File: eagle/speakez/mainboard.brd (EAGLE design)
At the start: 29 parts, among them U1 +12v

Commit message: added DAC cap + resistor
didn't choose cap value yet. Sent output to a header test pin
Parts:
- removed TESTPINS1: (no value), pinhead:1X05M
- added C9: (no value), SparkFun-Capacitors:0805
- added R5: 50k, SparkFun-Passives:0805
- TESTPINS: device pinhead:1X05M -> pinhead:1X07
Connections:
- new net N$27: C9.2, U$1.18
- new net N$28: C9.1, R5.2, TESTPINS.7
- net GND: now also R5.1, TESTPINS.6
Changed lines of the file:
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@@
 <element name="R1" library="rcl" package="M0805" value="5kohm" x="63.5" y="36.83"/>
 <element name="R2" library="rcl" package="M0805" value="5kohm" x="63.5" y="31.75"/>
-<element name="TESTPINS" library="pinhead" package="1X05M" value="" x="58.42" y="39.37" rot="R90"/>
+<element name="TESTPINS" library="pinhead" package="1X07" value="" x="58.42" y="39.37" rot="R90"/>
 <element name="TOAMBIENT" library="pinhead" package="1X04M" value="" x="63.5" y="46.99"/>
 <element name="VOICE" library="InvenSense-INMP621ACEZ-R7" package="ADI_ADMP521A" value="ADMP621ACEZ-RL7" x="63.5" y="17.78">
@@
 </element>
 <element name="C3" library="SparkFun-Capacitors" package="0805" value="0.1uF" x="-22.86" y="6.35"/>
-<element name="TESTPINS1" library="pinhead" package="1X05M" value="" x="-16.51" y="0"/>
 <element name="U$1" library="Teensy_DIY_v1.0" package="QFP50P1200X1200X160-64N" value="MK20DX256VLH7" x="-20.32" y="-15.24"/>
 <element name="JP1" library="pinhead" package="1X16" value="" x="0" y="-30.48"/>
@@
 <element name="PROGRAMMER" library="pel_hdr" package="PH005-1-5" value="PH1X5-05" x="-55.88" y="-95.25"/>
 <element name="SERIAL" library="pinhead" package="1X04" value="" x="-50.8" y="-109.22"/>
+<element name="R5" library="SparkFun-Passives" package="0805" value="50k" x="-64.77" y="-114.3"/>
+<element name="C9" library="SparkFun-Capacitors" package="0805" value="" x="-68.58" y="-114.3"/>
 </elements>
 <signals>
@@
 <contactref element="R1" pad="2"/>
 <contactref element="C1" pad="1"/>
-<contactref element="TESTPINS" pad="4"/>
 <contactref element="U$1" pad="38"/>
 <contactref element="U$1" pad="11"/>
-<wire x1="58.42" y1="41.37" x2="62.55" y2="41.91" width="0" layer="19" extent="1-1"/>
+<contactref element="TESTPINS" pad="4"/>
+<wire x1="58.42" y1="39.37" x2="62.55" y2="41.91" width="0" layer="19" extent="1-1"/>
 <wire x1="64.45" y1="36.83" x2="62.55" y2="41.91" width="0" layer="19" extent="1-1"/>
-<wire x1="-14.605" y1="-16.4846" x2="58.42" y2="41.37" width="0" layer="19" extent="1-1"/>
+<wire x1="-14.605" y1="-16.4846" x2="58.42" y2="39.37" width="0" layer="19" extent="1-1"/>
 <wire x1="-26.035" y1="-16.4846" x2="-14.605" y2="-16.4846" width="0" layer="19" extent="1-1"/>
 </signal>
@@
 <contactref element="R2" pad="2"/>
 <contactref element="C2" pad="1"/>
-<contactref element="TESTPINS" pad="5"/>
 <contactref element="U$1" pad="37"/>
 <contactref element="U$1" pad="12"/>
-<wire x1="64.45" y1="31.75" x2="58.42" y2="43.37" width="0" layer="19" extent="1-1"/>
+<contactref element="TESTPINS" pad="5"/>
+<wire x1="64.45" y1="31.75" x2="58.42" y2="41.91" width="0" layer="19" extent="1-1"/>
 <wire x1="62.55" y1="26.67" x2="64.45" y2="31.75" width="0" layer="19" extent="1-1"/>
 <wire x1="-14.605" y1="-16.9926" x2="62.55" y2="26.67" width="0" layer="19" extent="1-1"/>
@@
 <contactref element="TOAMBIENT" pad="3"/>
 <contactref element="R3" pad="1"/>
+<contactref element="R5" pad="1"/>
+<contactref element="TESTPINS" pad="6"/>
+<wire x1="-58.05" y1="-86.36" x2="-65.67" y2="-114.3" width="0" layer="19" extent="1-1"/>
 <wire x1="61.7728" y1="17.78" x2="-58.05" y2="-86.36" width="0" layer="19" extent="1-1"/>
 <wire x1="62.5348" y1="17.78" x2="61.7728" y2="17.78" width="0" layer="19" extent="1-1"/>
@@
 <wire x1="64.45" y1="41.91" x2="64.45" y2="26.67" width="0" layer="19" extent="1-1"/>
 <wire x1="64.5" y1="46.99" x2="64.45" y2="41.91" width="0" layer="19" extent="1-1"/>
+<wire x1="58.42" y1="44.45" x2="64.45" y2="41.91" width="0" layer="19" extent="1-1"/>
 </signal>
 <signal name="N$4">
 <contactref element="VOICE" pad="5"/>
 <contactref element="R2" pad="1"/>
-<contactref element="TESTPINS" pad="3"/>
 <contactref element="U$1" pad="36"/>
 <contactref element="U$1" pad="9"/>
-<wire x1="62.55" y1="31.75" x2="58.42" y2="39.37" width="0" layer="19" extent="1-1"/>
+<contactref element="TESTPINS" pad="3"/>
+<wire x1="62.55" y1="31.75" x2="58.42" y2="36.83" width="0" layer="19" extent="1-1"/>
 <wire x1="64.6176" y1="17.3228" x2="62.55" y2="31.75" width="0" layer="19" extent="1-1"/>
 <wire x1="-14.605" y1="-17.5006" x2="64.6176" y2="17.3228" width="0" layer="19" extent="1-1"/>
@@
 </signal>
 <signal name="TEST-PINS">
-<contactref element="TESTPINS" pad="1"/>
 <contactref element="VOICE" pad="1"/>
 <contactref element="TOAMBIENT" pad="2"/>
-<wire x1="58.42" y1="35.37" x2="62.5" y2="46.99" width="0" layer="19" extent="1-1"/>
-<wire x1="64.6176" y1="18.2372" x2="58.42" y2="35.37" width="0" layer="19" extent="1-1"/>
+<contactref element="TESTPINS" pad="1"/>
+<wire x1="58.42" y1="31.75" x2="62.5" y2="46.99" width="0" layer="19" extent="1-1"/>
+<wire x1="64.6176" y1="18.2372" x2="58.42" y2="31.75" width="0" layer="19" extent="1-1"/>
 </signal>
 <signal name="N$5">
@@
 <signal name="N$10">
 <contactref element="TOAMBIENT" pad="4"/>
-<contactref element="TESTPINS" pad="2"/>
 <contactref element="R1" pad="1"/>
 <contactref element="U$1" pad="10"/>
+<contactref element="TESTPINS" pad="2"/>
 <wire x1="62.55" y1="36.83" x2="66.5" y2="46.99" width="0" layer="19" extent="1-1"/>
-<wire x1="58.42" y1="37.37" x2="62.55" y2="36.83" width="0" layer="19" extent="1-1"/>
-<wire x1="-26.035" y1="-16.002" x2="58.42" y2="37.37" width="0" layer="19" extent="1-1"/>
+<wire x1="58.42" y1="34.29" x2="62.55" y2="36.83" width="0" layer="19" extent="1-1"/>
+<wire x1="-26.035" y1="-16.002" x2="58.42" y2="34.29" width="0" layer="19" extent="1-1"/>
 </signal>
 <signal name="N$9">
@@
 <wire x1="-26.035" y1="-11.9888" x2="-52.07" y2="-109.22" width="0" layer="19" extent="1-1"/>
 </signal>
+<signal name="N$27">
+<contactref element="U$1" pad="18"/>
+<contactref element="C9" pad="2"/>
+<wire x1="-23.5712" y1="-20.955" x2="-67.68" y2="-114.3" width="0" layer="19" extent="1-1"/>
+</signal>
+<signal name="N$28">
+<contactref element="C9" pad="1"/>
+<contactref element="R5" pad="2"/>
+<contactref element="TESTPINS" pad="7"/>
+<wire x1="-63.87" y1="-114.3" x2="-69.48" y2="-114.3" width="0" layer="19" extent="1-1"/>
+<wire x1="58.42" y1="46.99" x2="-63.87" y2="-114.3" width="0" layer="19" extent="1-1"/>
+</signal>
 </signals>

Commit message: test pins for VCC and RESET
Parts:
- removed JP1, JP2, JP3, JP4: (no value), pinhead:1X16
- added TEST2: (no value), pinhead:1X05
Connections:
- net N$16: now also TEST2.1
- net N$20: now also TEST2.2
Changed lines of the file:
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@@
 <element name="C3" library="SparkFun-Capacitors" package="0805" value="0.1uF" x="-22.86" y="6.35"/>
 <element name="U$1" library="Teensy_DIY_v1.0" package="QFP50P1200X1200X160-64N" value="MK20DX256VLH7" x="-20.32" y="-15.24"/>
-<element name="JP1" library="pinhead" package="1X16" value="" x="0" y="-30.48"/>
-<element name="JP2" library="pinhead" package="1X16" value="" x="0" y="-45.72"/>
-<element name="JP3" library="pinhead" package="1X16" value="" x="0" y="-60.96"/>
-<element name="JP4" library="pinhead" package="1X16" value="" x="0" y="-76.2"/>
 <element name="U1" library="SparkFun-PowerIC" package="TO-252" value="+12v" x="-34.29" y="-74.93">
 <attribute name="PROD_ID" value="VREG-12370" x="-34.29" y="-74.93" size="1.778" layer="27" display="off"/>
@@
 <element name="R5" library="SparkFun-Passives" package="0805" value="50k" x="-64.77" y="-114.3"/>
 <element name="C9" library="SparkFun-Capacitors" package="0805" value="" x="-68.58" y="-114.3"/>
+<element name="TEST2" library="pinhead" package="1X05" value="" x="-57.15" y="-124.46"/>
 </elements>
 <signals>
@@
 <contactref element="R4" pad="1"/>
 <contactref element="SERIAL" pad="3"/>
+<contactref element="TEST2" pad="1"/>
+<wire x1="-49.53" y1="-109.22" x2="-62.23" y2="-124.46" width="0" layer="19" extent="1-1"/>
 <wire x1="-61.86" y1="-86.36" x2="-49.53" y2="-109.22" width="0" layer="19" extent="1-1"/>
 <wire x1="-54.24" y1="-81.28" x2="-61.86" y2="-86.36" width="0" layer="19" extent="1-1"/>
@@
 <contactref element="R4" pad="2"/>
 <contactref element="PROGRAMMER" pad="1"/>
+<contactref element="TEST2" pad="2"/>
+<wire x1="-55.88" y1="-95.25" x2="-59.69" y2="-124.46" width="0" layer="19" extent="1-1"/>
 <wire x1="-60.06" y1="-86.36" x2="-55.88" y2="-95.25" width="0" layer="19" extent="1-1"/>
 <wire x1="-14.605" y1="-18.4912" x2="-60.06" y2="-86.36" width="0" layer="19" extent="1-1"/>

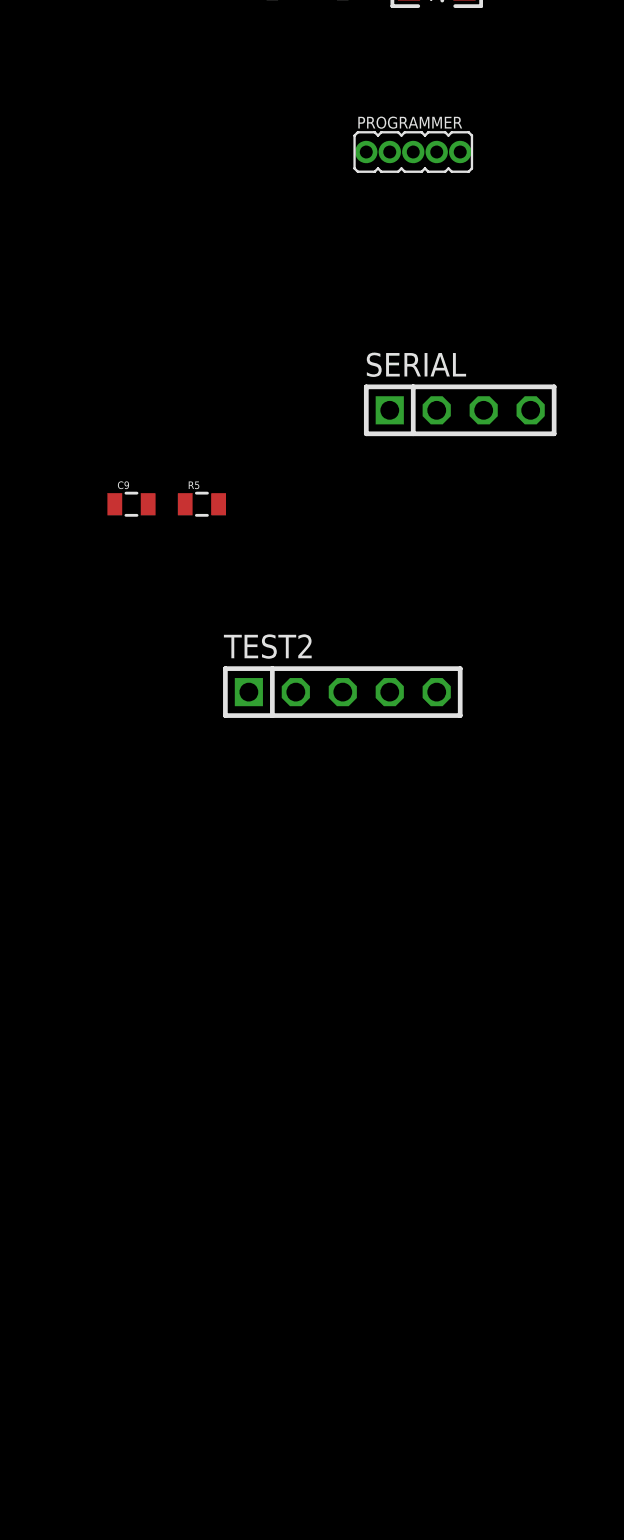
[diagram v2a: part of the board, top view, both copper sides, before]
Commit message: Added correct header for programmer
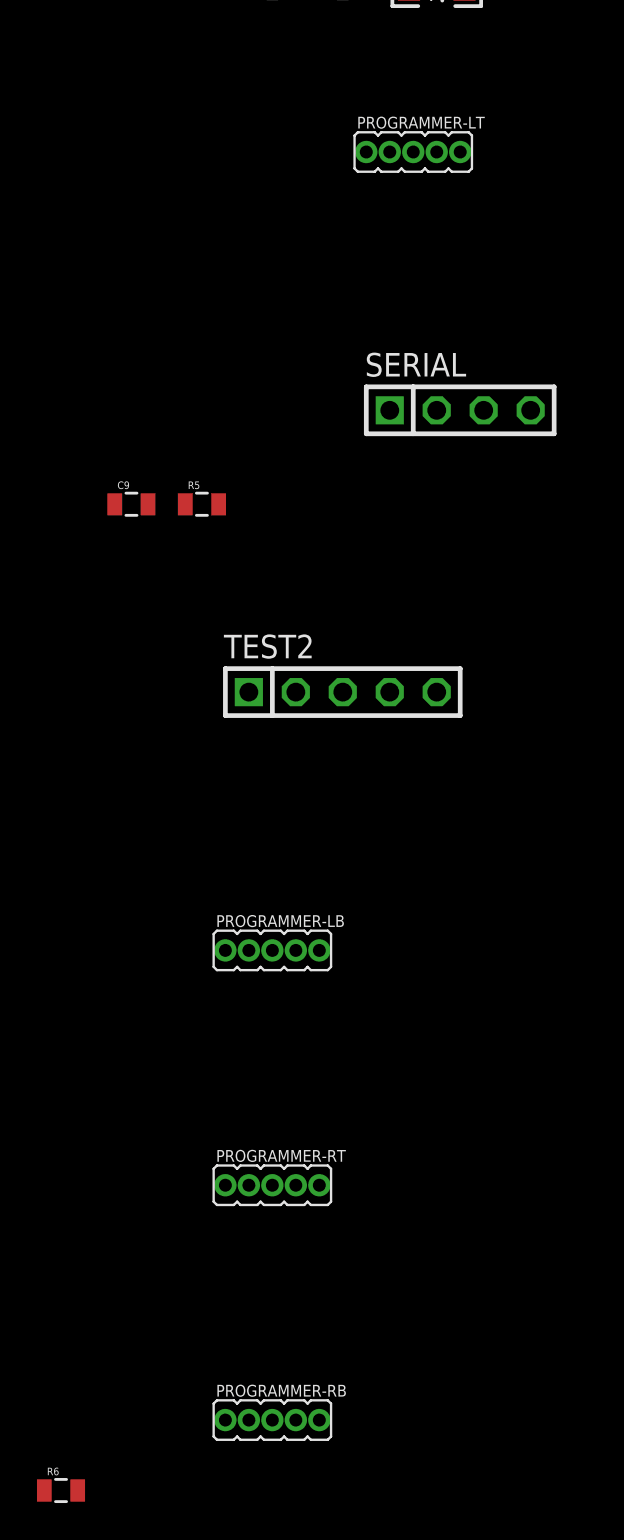
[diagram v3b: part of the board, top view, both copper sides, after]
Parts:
- added PROGRAMMER-LB, PROGRAMMER-RB, PROGRAMMER-RT: PH1X5-05, pel_hdr:PH005-1-5
- added R6: 100k, SparkFun-Passives:0805
- renumbered PROGRAMMER to PROGRAMMER-LT
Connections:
- removed net N$22: PROGRAMMER-LT.3, U$1.23
- new net N$29: BATTERY.2, C6.2, C7.2, C8.2, PROGRAMMER-RB.1, PROGRAMMER-RB.2, PROGRAMMER-RB.3, PROGRAMMER-RB.4, PROGRAMMER-RB.5, PROGRAMMER-RT.2, PROGRAMMER-RT.3, PROGRAMMER-RT.4, PROGRAMMER-RT.5, SERIAL.4, U$1.31, U$1.4, U$1.47, U1.3
- net N$14: now also PROGRAMMER-LT.5, U$1.22; no longer BATTERY.2, C6.2, C7.2, C8.2, SERIAL.4, U$1.31, U$1.4, U$1.47, U1.3
- net N$16: now also PROGRAMMER-LT.1, R6.1
- net N$20: now also PROGRAMMER-LB.3; no longer PROGRAMMER-LT.1
- net N$21: now also PROGRAMMER-LB.4, U$1.23; no longer PROGRAMMER-LT.2, U$1.22
- net N$23: now also PROGRAMMER-LT.3; no longer PROGRAMMER-LT.4
- net N$24: now also PROGRAMMER-LT.4, R6.2; no longer PROGRAMMER-LT.5
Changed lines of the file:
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@@
 <element name="R3" library="SparkFun-Passives" package="0805" value="66 ohms" x="-57.15" y="-86.36"/>
 <element name="R4" library="SparkFun-Passives" package="0805" value="10k" x="-60.96" y="-86.36"/>
-<element name="PROGRAMMER" library="pel_hdr" package="PH005-1-5" value="PH1X5-05" x="-55.88" y="-95.25"/>
+<element name="PROGRAMMER-LT" library="pel_hdr" package="PH005-1-5" value="PH1X5-05" x="-55.88" y="-95.25"/>
 <element name="SERIAL" library="pinhead" package="1X04" value="" x="-50.8" y="-109.22"/>
 <element name="R5" library="SparkFun-Passives" package="0805" value="50k" x="-64.77" y="-114.3"/>
 <element name="C9" library="SparkFun-Capacitors" package="0805" value="" x="-68.58" y="-114.3"/>
 <element name="TEST2" library="pinhead" package="1X05" value="" x="-57.15" y="-124.46"/>
+<element name="PROGRAMMER-LB" library="pel_hdr" package="PH005-1-5" value="PH1X5-05" x="-63.5" y="-138.43"/>
+<element name="PROGRAMMER-RT" library="pel_hdr" package="PH005-1-5" value="PH1X5-05" x="-63.5" y="-151.13"/>
+<element name="PROGRAMMER-RB" library="pel_hdr" package="PH005-1-5" value="PH1X5-05" x="-63.5" y="-163.83"/>
+<element name="R6" library="SparkFun-Passives" package="0805" value="100k" x="-72.39" y="-167.64"/>
 </elements>
 <signals>
@@
 <wire x1="80.975" y1="40.64" x2="77.2" y2="43.18" width="0" layer="19" extent="1-1"/>
 </signal>
-<signal name="N$14">
-<contactref element="BATTERY" pad="2"/>
-<contactref element="U1" pad="3"/>
-<contactref element="C6" pad="2"/>
-<contactref element="U$1" pad="31"/>
-<contactref element="U$1" pad="47"/>
-<contactref element="U$1" pad="4"/>
-<contactref element="C7" pad="2"/>
-<contactref element="C8" pad="2"/>
-<contactref element="SERIAL" pad="4"/>
-<wire x1="-48.63" y1="-81.28" x2="-46.99" y2="-109.22" width="0" layer="19" extent="1-1"/>
-<wire x1="-52.44" y1="-81.28" x2="-48.63" y2="-81.28" width="0" layer="19" extent="1-1"/>
-<wire x1="-44.82" y1="-81.28" x2="-48.63" y2="-81.28" width="0" layer="19" extent="1-1"/>
-<wire x1="-34.29" y1="-72.43" x2="-44.82" y2="-81.28" width="0" layer="19" extent="1-1"/>
-<wire x1="-17.0688" y1="-20.955" x2="-34.29" y2="-72.43" width="0" layer="19" extent="1-1"/>
-<wire x1="-14.605" y1="-11.9888" x2="-17.0688" y2="-20.955" width="0" layer="19" extent="1-1"/>
-<wire x1="-26.035" y1="-12.9794" x2="-14.605" y2="-11.9888" width="0" layer="19" extent="1-1"/>
-<wire x1="75.2" y1="43.18" x2="-14.605" y2="-11.9888" width="0" layer="19" extent="1-1"/>
-</signal>
 <signal name="N$15">
 <contactref element="U1" pad="1"/>
@@
 <contactref element="SERIAL" pad="3"/>
 <contactref element="TEST2" pad="1"/>
+<contactref element="PROGRAMMER-LT" pad="1"/>
+<contactref element="R6" pad="1"/>
+<wire x1="-62.23" y1="-124.46" x2="-73.29" y2="-167.64" width="0" layer="19" extent="1-1"/>
 <wire x1="-49.53" y1="-109.22" x2="-62.23" y2="-124.46" width="0" layer="19" extent="1-1"/>
-<wire x1="-61.86" y1="-86.36" x2="-49.53" y2="-109.22" width="0" layer="19" extent="1-1"/>
+<wire x1="-55.88" y1="-95.25" x2="-49.53" y2="-109.22" width="0" layer="19" extent="1-1"/>
+<wire x1="-61.86" y1="-86.36" x2="-55.88" y2="-95.25" width="0" layer="19" extent="1-1"/>
 <wire x1="-54.24" y1="-81.28" x2="-61.86" y2="-86.36" width="0" layer="19" extent="1-1"/>
 <wire x1="-46.62" y1="-81.28" x2="-54.24" y2="-81.28" width="0" layer="19" extent="1-1"/>
@@
 <contactref element="U$1" pad="34"/>
 <contactref element="R4" pad="2"/>
-<contactref element="PROGRAMMER" pad="1"/>
 <contactref element="TEST2" pad="2"/>
-<wire x1="-55.88" y1="-95.25" x2="-59.69" y2="-124.46" width="0" layer="19" extent="1-1"/>
-<wire x1="-60.06" y1="-86.36" x2="-55.88" y2="-95.25" width="0" layer="19" extent="1-1"/>
+<contactref element="PROGRAMMER-LB" pad="3"/>
+<wire x1="-59.69" y1="-124.46" x2="-60.96" y2="-138.43" width="0" layer="19" extent="1-1"/>
+<wire x1="-60.06" y1="-86.36" x2="-59.69" y2="-124.46" width="0" layer="19" extent="1-1"/>
 <wire x1="-14.605" y1="-18.4912" x2="-60.06" y2="-86.36" width="0" layer="19" extent="1-1"/>
-</signal>
-<signal name="N$21">
-<contactref element="U$1" pad="22"/>
-<contactref element="PROGRAMMER" pad="2"/>
-<wire x1="-21.5646" y1="-20.955" x2="-54.61" y2="-95.25" width="0" layer="19" extent="1-1"/>
-</signal>
-<signal name="N$22">
-<contactref element="U$1" pad="23"/>
-<contactref element="PROGRAMMER" pad="3"/>
-<wire x1="-21.082" y1="-20.955" x2="-53.34" y2="-95.25" width="0" layer="19" extent="1-1"/>
 </signal>
 <signal name="N$23">
 <contactref element="U$1" pad="24"/>
-<contactref element="PROGRAMMER" pad="4"/>
-<wire x1="-20.574" y1="-20.955" x2="-52.07" y2="-95.25" width="0" layer="19" extent="1-1"/>
+<contactref element="PROGRAMMER-LT" pad="3"/>
+<wire x1="-20.574" y1="-20.955" x2="-53.34" y2="-95.25" width="0" layer="19" extent="1-1"/>
 </signal>
 <signal name="N$24">
 <contactref element="U$1" pad="25"/>
-<contactref element="PROGRAMMER" pad="5"/>
-<wire x1="-20.066" y1="-20.955" x2="-50.8" y2="-95.25" width="0" layer="19" extent="1-1"/>
+<contactref element="PROGRAMMER-LT" pad="4"/>
+<contactref element="R6" pad="2"/>
+<wire x1="-52.07" y1="-95.25" x2="-71.49" y2="-167.64" width="0" layer="19" extent="1-1"/>
+<wire x1="-20.066" y1="-20.955" x2="-52.07" y2="-95.25" width="0" layer="19" extent="1-1"/>
 </signal>
 <signal name="N$25">
@@
 <wire x1="58.42" y1="46.99" x2="-63.87" y2="-114.3" width="0" layer="19" extent="1-1"/>
 </signal>
+<signal name="N$29">
+<contactref element="PROGRAMMER-RT" pad="2"/>
+<contactref element="PROGRAMMER-RT" pad="3"/>
+<contactref element="PROGRAMMER-RT" pad="4"/>
+<contactref element="PROGRAMMER-RT" pad="5"/>
+<contactref element="PROGRAMMER-RB" pad="1"/>
+<contactref element="PROGRAMMER-RB" pad="2"/>
+<contactref element="PROGRAMMER-RB" pad="3"/>
+<contactref element="PROGRAMMER-RB" pad="4"/>
+<contactref element="PROGRAMMER-RB" pad="5"/>
+<contactref element="BATTERY" pad="2"/>
+<contactref element="U1" pad="3"/>
+<contactref element="C6" pad="2"/>
+<contactref element="U$1" pad="31"/>
+<contactref element="U$1" pad="47"/>
+<contactref element="U$1" pad="4"/>
+<contactref element="C7" pad="2"/>
+<contactref element="C8" pad="2"/>
+<contactref element="SERIAL" pad="4"/>
+<wire x1="-62.23" y1="-163.83" x2="-63.5" y2="-163.83" width="0" layer="19" extent="1-1"/>
+<wire x1="-60.96" y1="-163.83" x2="-62.23" y2="-163.83" width="0" layer="19" extent="1-1"/>
+<wire x1="-59.69" y1="-163.83" x2="-60.96" y2="-163.83" width="0" layer="19" extent="1-1"/>
+<wire x1="-58.42" y1="-163.83" x2="-59.69" y2="-163.83" width="0" layer="19" extent="1-1"/>
+<wire x1="-62.23" y1="-151.13" x2="-62.23" y2="-163.83" width="0" layer="19" extent="1-1"/>
+<wire x1="-60.96" y1="-151.13" x2="-62.23" y2="-151.13" width="0" layer="19" extent="1-1"/>
+<wire x1="-59.69" y1="-151.13" x2="-60.96" y2="-151.13" width="0" layer="19" extent="1-1"/>
+<wire x1="-58.42" y1="-151.13" x2="-59.69" y2="-151.13" width="0" layer="19" extent="1-1"/>
+<wire x1="-46.99" y1="-109.22" x2="-58.42" y2="-151.13" width="0" layer="19" extent="1-1"/>
+<wire x1="-48.63" y1="-81.28" x2="-46.99" y2="-109.22" width="0" layer="19" extent="1-1"/>
+<wire x1="-52.44" y1="-81.28" x2="-48.63" y2="-81.28" width="0" layer="19" extent="1-1"/>
+<wire x1="-44.82" y1="-81.28" x2="-48.63" y2="-81.28" width="0" layer="19" extent="1-1"/>
+<wire x1="-34.29" y1="-72.43" x2="-44.82" y2="-81.28" width="0" layer="19" extent="1-1"/>
+<wire x1="-17.0688" y1="-20.955" x2="-34.29" y2="-72.43" width="0" layer="19" extent="1-1"/>
+<wire x1="-14.605" y1="-11.9888" x2="-17.0688" y2="-20.955" width="0" layer="19" extent="1-1"/>
+<wire x1="-26.035" y1="-12.9794" x2="-14.605" y2="-11.9888" width="0" layer="19" extent="1-1"/>
+<wire x1="75.2" y1="43.18" x2="-14.605" y2="-11.9888" width="0" layer="19" extent="1-1"/>
+</signal>
+<signal name="N$14">
+<contactref element="U$1" pad="22"/>
+<contactref element="PROGRAMMER-LT" pad="5"/>
+<wire x1="-21.5646" y1="-20.955" x2="-50.8" y2="-95.25" width="0" layer="19" extent="1-1"/>
+</signal>
+<signal name="N$21">
+<contactref element="U$1" pad="23"/>
+<contactref element="PROGRAMMER-LB" pad="4"/>
+<wire x1="-21.082" y1="-20.955" x2="-59.69" y2="-138.43" width="0" layer="19" extent="1-1"/>
+</signal>
 </signals>
